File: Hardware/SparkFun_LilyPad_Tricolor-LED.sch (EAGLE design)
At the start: 17 parts

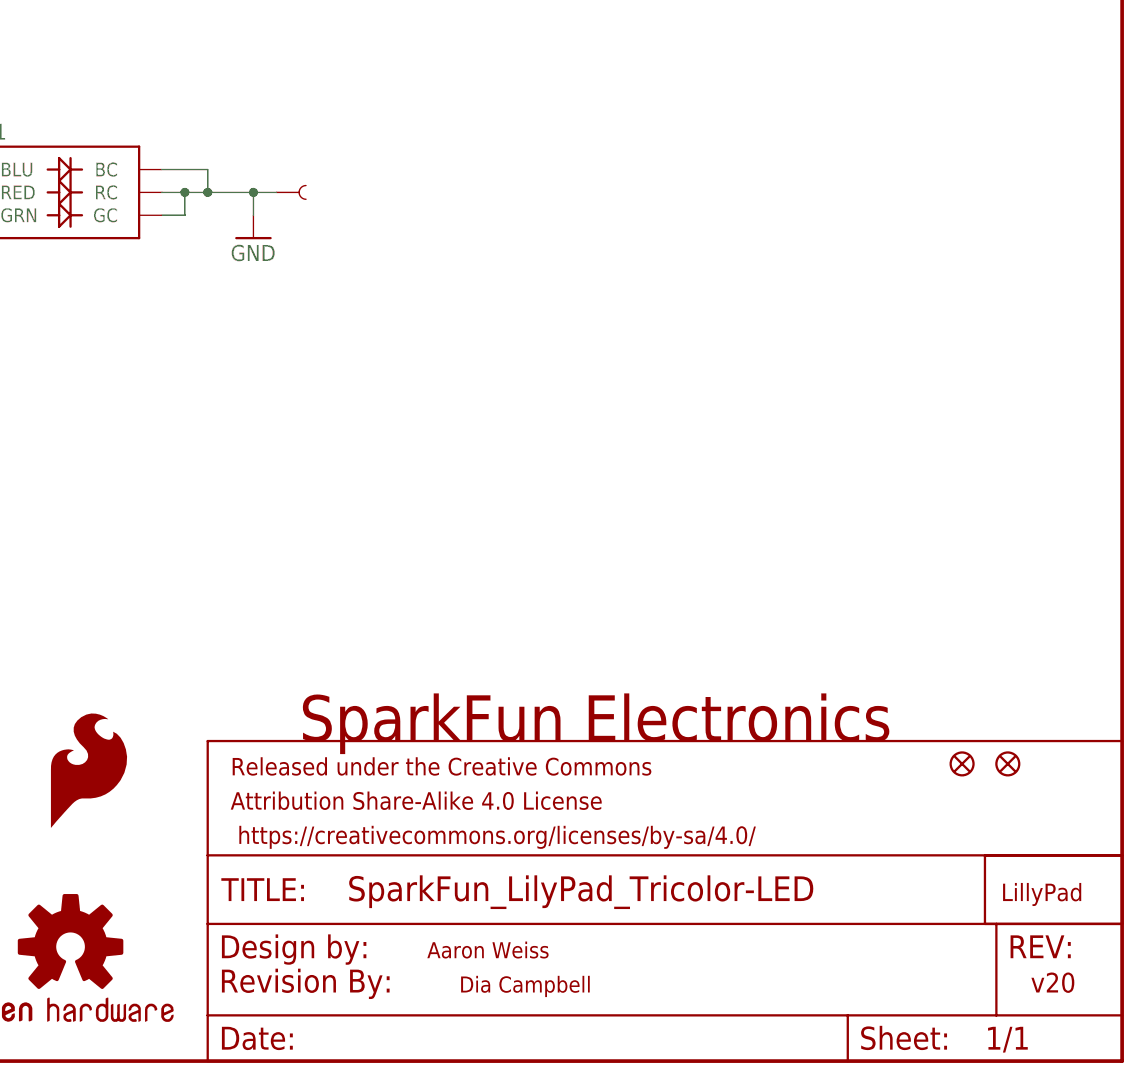
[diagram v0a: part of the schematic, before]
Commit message: Checklist tweaks to the schematic
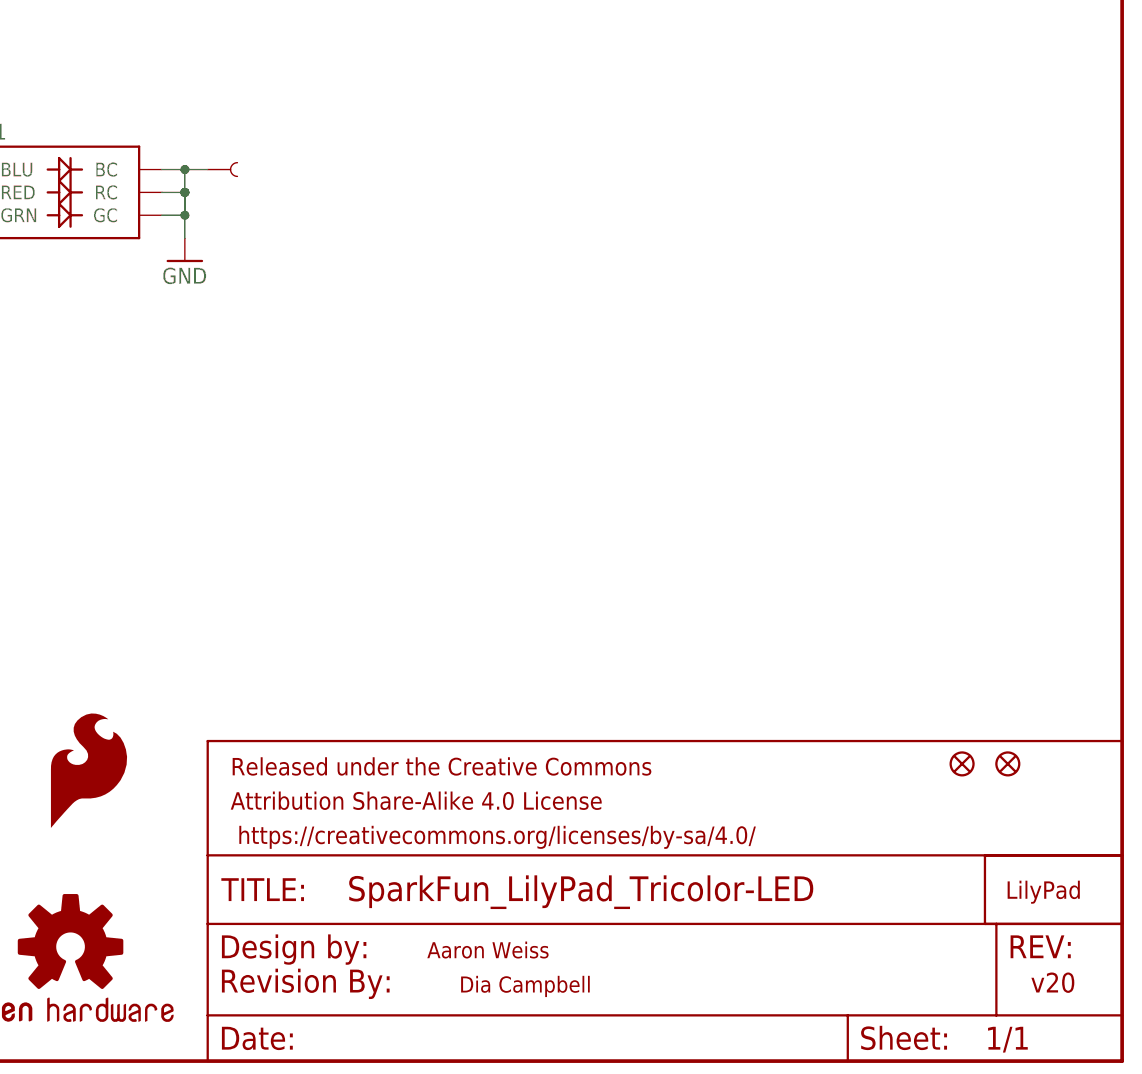
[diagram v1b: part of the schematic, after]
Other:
- note removed: "SparkFun Electronics"
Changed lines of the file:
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@@
 <sheet>
 <plain>
-<text x="157.48" y="35.56" size="5.08" layer="94">SparkFun Electronics</text>
 <text x="238.76" y="7.62" size="2.1844" layer="94">v20</text>
 <text x="171.704" y="11.43" size="1.778" layer="94">Aaron Weiss</text>
@@
 <instance part="BLU" gate="G$1" x="96.52" y="104.14" smashed="yes" rot="R180"/>
 <instance part="RED" gate="G$1" x="96.52" y="96.52" smashed="yes" rot="R180"/>
-<instance part="GND" gate="G$1" x="157.48" y="96.52" smashed="yes"/>
+<instance part="GND" gate="G$1" x="149.86" y="99.06" smashed="yes"/>
 <instance part="U$2" gate="G$1" x="68.58" y="73.66" rot="R180"/>
 <instance part="U$3" gate="G$1" x="68.58" y="71.12" rot="R180"/>
@@
 <instance part="FID1" gate="G$1" x="231.14" y="33.02"/>
 <instance part="FID2" gate="G$1" x="236.22" y="33.02"/>
-<instance part="GND1" gate="1" x="152.4" y="91.44"/>
+<instance part="GND1" gate="1" x="144.78" y="88.9"/>
 <instance part="U$4" gate="G$1" x="148.59" y="7.62"/>
 </instances>
@@
 <wire x1="142.24" y1="96.52" x2="144.78" y2="96.52" width="0.1524" layer="91"/>
 <pinref part="D1" gate="G$1" pin="GC"/>
-<wire x1="144.78" y1="96.52" x2="147.32" y2="96.52" width="0.1524" layer="91"/>
 <wire x1="142.24" y1="93.98" x2="144.78" y2="93.98" width="0.1524" layer="91"/>
-<wire x1="144.78" y1="93.98" x2="144.78" y2="96.52" width="0.1524" layer="91"/>
 <junction x="144.78" y="96.52"/>
 <pinref part="D1" gate="G$1" pin="BC"/>
-<wire x1="142.24" y1="99.06" x2="147.32" y2="99.06" width="0.1524" layer="91"/>
-<wire x1="147.32" y1="99.06" x2="147.32" y2="96.52" width="0.1524" layer="91"/>
-<junction x="147.32" y="96.52"/>
-<wire x1="147.32" y1="96.52" x2="152.4" y2="96.52" width="0.1524" layer="91"/>
+<wire x1="142.24" y1="99.06" x2="144.78" y2="99.06" width="0.1524" layer="91"/>
+<wire x1="144.78" y1="99.06" x2="144.78" y2="96.52" width="0.1524" layer="91"/>
+<junction x="144.78" y="96.52"/>
+<wire x1="144.78" y1="96.52" x2="144.78" y2="93.98" width="0.1524" layer="91"/>
 <pinref part="GND1" gate="1" pin="GND"/>
-<wire x1="152.4" y1="93.98" x2="152.4" y2="96.52" width="0.1524" layer="91"/>
+<wire x1="144.78" y1="91.44" x2="144.78" y2="93.98" width="0.1524" layer="91"/>
 <pinref part="GND" gate="G$1" pin="1"/>
-<wire x1="152.4" y1="96.52" x2="154.94" y2="96.52" width="0.1524" layer="91"/>
-<junction x="152.4" y="96.52"/>
+<wire x1="144.78" y1="93.98" x2="144.78" y2="96.52" width="0.1524" layer="91"/>
+<wire x1="144.78" y1="99.06" x2="147.32" y2="99.06" width="0.1524" layer="91"/>
+<junction x="144.78" y="93.98"/>
+<junction x="144.78" y="99.06"/>
 </segment>
 </net>

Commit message: Changes to meet new design standards
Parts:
- LOGO1: value OSHW-LOGOS-COPPER -> OSHW-LOGOS; device SparkFun-Aesthetics:OSHW-LOGOS-COPPER -> SparkFun-Aesthetics:OSHW-LOGOS
- LOGO2: value SFE_LOGO_FLAME.1COP -> SFE_LOGO_FLAME.1_INCH; device SparkFun-Aesthetics:SFE_LOGO_FLAME.1COP -> SparkFun-Aesthetics:SFE_LOGO_FLAME.1_INCH
- U$1: value LOGO-LPL -> LOGO-LPLP; device LilyPad-Wearables:LOGO-LPL -> LilyPad-Wearables:LOGO-LPLP
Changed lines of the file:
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@@
 <part name="U$2" library="LilyPad-Wearables" deviceset="SEWTAP-NOHOLE" device="2"/>
 <part name="U$3" library="LilyPad-Wearables" deviceset="SEWTAP-NOHOLE" device="2"/>
-<part name="U$1" library="LilyPad-Wearables" deviceset="LOGO-LP" device="L"/>
-<part name="LOGO1" library="SparkFun-Aesthetics" deviceset="OSHW-LOGO" device="S-COPPER"/>
-<part name="LOGO2" library="SparkFun-Aesthetics" deviceset="SFE_LOGO_FLAME" device=".1COP"/>
+<part name="U$1" library="LilyPad-Wearables" deviceset="LOGO-LP" device="LP" value="LOGO-LPLP"/>
+<part name="LOGO1" library="SparkFun-Aesthetics" deviceset="OSHW-LOGO" device="S" value="OSHW-LOGOS"/>
+<part name="LOGO2" library="SparkFun-Aesthetics" deviceset="SFE_LOGO_FLAME" device=".1_INCH" value="SFE_LOGO_FLAME.1_INCH"/>
 <part name="FID1" library="SparkFun-Aesthetics" deviceset="FIDUCIAL" device="1X2"/>
 <part name="FID2" library="SparkFun-Aesthetics" deviceset="FIDUCIAL" device="1X2"/>
